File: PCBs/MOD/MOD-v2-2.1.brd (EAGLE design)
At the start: 138.8 x 49.3 mm, 38 parts, among them J1 SERVO1, J10 JOY1, J11 JOY2, J12 RPi-Reset, J2 SERVO2, J3 RPi, J4 ACTUATORS, J5 Battery, J6 AN5, J7 AN6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

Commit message: new MOD pcb
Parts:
- added C1: 10uF, resistor:C0805
- added J13: AN5, SparkFun-Connectors:1X03_LOCK
- added J14: AN6, SparkFun-Connectors:1X03_LOCK
- added J15: AN7, SparkFun-Connectors:1X03_LOCK
- added J16: AN8, SparkFun-Connectors:1X03_LOCK
- J12: value RPi-Reset -> RPi-Shutdown
- J6, J7, J8, J9: device SparkFun-Connectors:1X03_NO_SILK -> SparkFun-Connectors:1X03_LOCK
- R1: device resistor:0204/7 -> rcl:M0805
- R2: value 2.2k -> 2.2K; device resistor:0204/7 -> rcl:M0805
- R3: value 3.3k -> 3.3K; device resistor:0204/7 -> rcl:M0805
- U1: value ATTINY85SU -> ATTINY85
- moved J12 223.1 mm to (127.4, 31.4), flipped to the bottom, turned to 270 degrees
- moved J3 204.9 mm to (150.6, 28.9), turned to 90 degrees
- moved SW2 198.9 mm to (139.6, 7.70), turned to 270 degrees
- moved R3 196.8 mm to (118.1, 12.8), flipped to the bottom
- moved R2 188.3 mm to (118.1, 4.21), flipped to the bottom, turned to 180 degrees
- moved RELAY1 158.8 mm to (131.0, 28.0), flipped to the bottom, turned to 90 degrees
- moved U1 151.6 mm to (128.6, 20.4), flipped to the bottom, turned to 270 degrees
- moved J2 125.3 mm to (2.99, 24.0), flipped to the bottom
- moved J1 120.3 mm to (5.46, 24.0), flipped to the bottom
- moved J9 111.1 mm to (121.3, 34.4), turned to 0 degrees
- moved J4 100.4 mm to (11.0, 32.0)
- moved J8 97.8 mm to (111.1, 34.3), turned to 0 degrees
- moved J6 81.5 mm to (100.8, 34.3), turned to 0 degrees
- moved J7 74.3 mm to (90.5, 34.4), turned to 0 degrees
- moved LED1 70.9 mm to (139.7, 17.9)
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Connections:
- net +3V3: now also J13.1, J14.1, J15.1, J16.1
- net +5V: now also R1.1, TEENSY.VIN; no longer R1.2
- net +5V-BATTERY: now also C1.1
- net AGND: now also J13.2, J14.2, J15.2, J16.2, J6.2, J7.2, J8.2, J9.2; no longer J6.3, J7.3, J8.3, J9.3
- net AN10: now also J7.3
- net AN11: now also J8.3
- net AN12: now also J9.3
- net AN5: now also J13.3; no longer J6.2
- net AN6: now also J14.3; no longer J7.2
- net AN7: now also J15.3; no longer J8.2
- net AN8: now also J16.3; no longer J9.2
- net AN9: now also J6.3
- net GND: now also C1.2, R3.2; no longer R3.1
- net N$2: now also R1.2; no longer R1.1
- net N$5: now also R2.2, R3.1; no longer R2.1, R3.2
- net PI-REST: now also R2.1; no longer R2.2
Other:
- board size 138.8 x 49.3 mm -> 149.8 x 49.3 mm
- board text added: "MOL v2-2"
- board text removed: "MO v2-2"

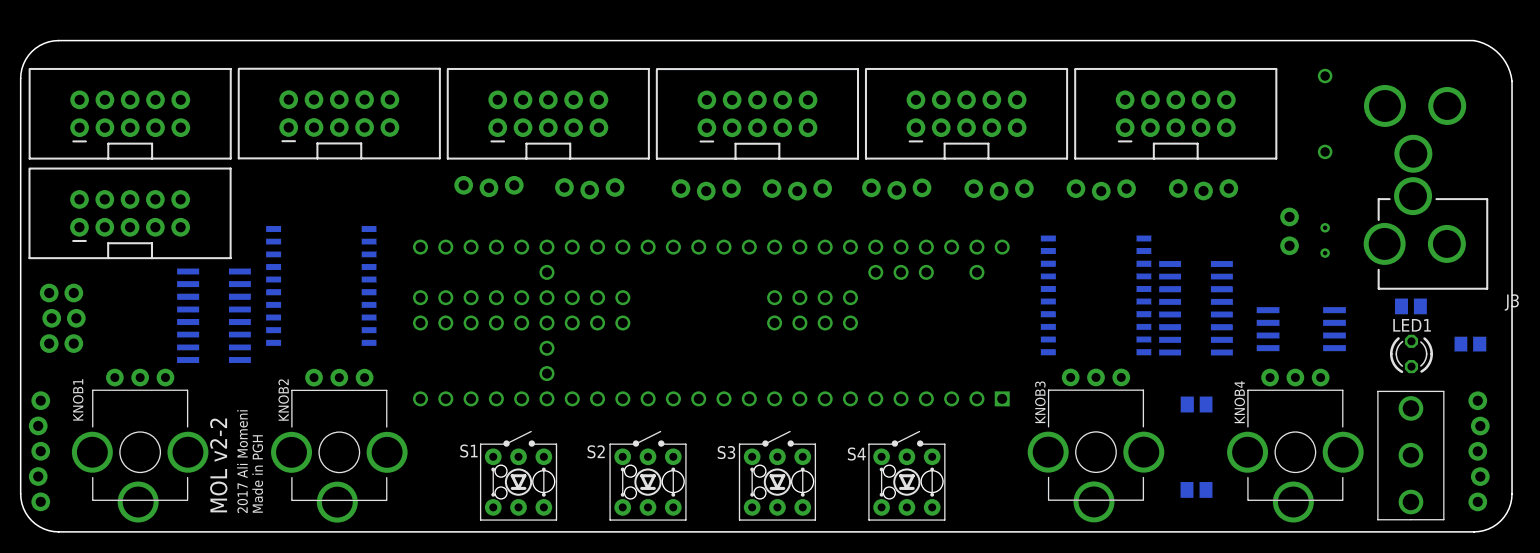
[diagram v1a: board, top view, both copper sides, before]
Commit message: routed new MOD pcb v2-2.1
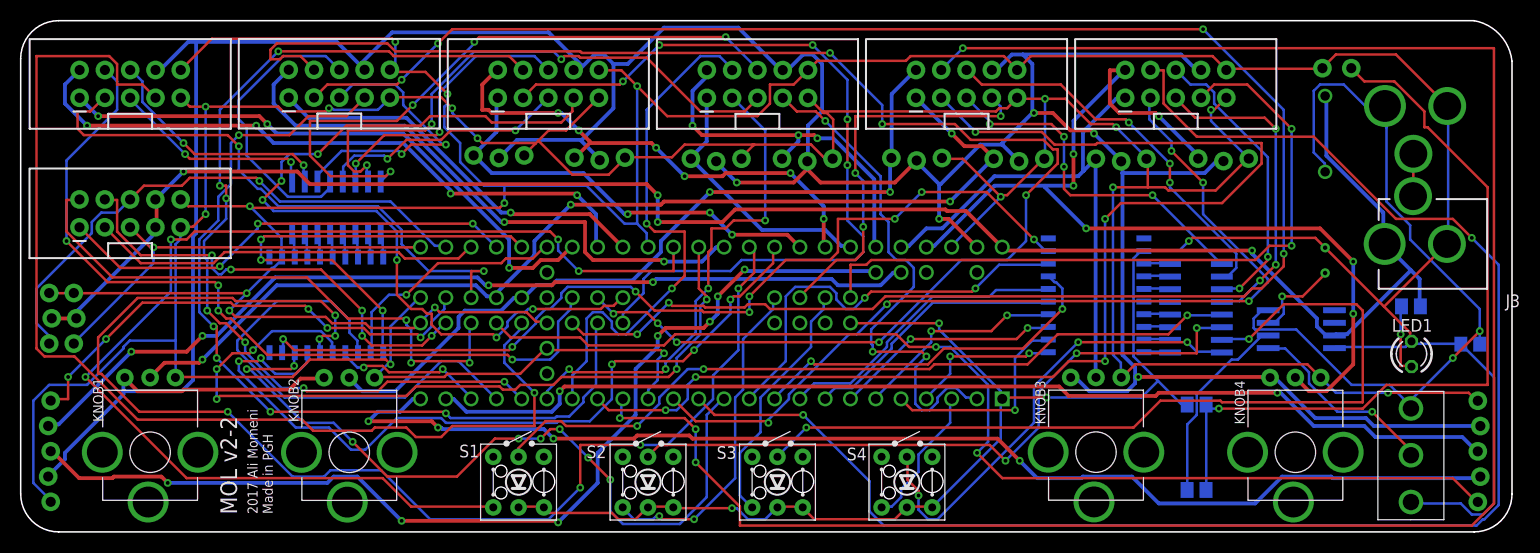
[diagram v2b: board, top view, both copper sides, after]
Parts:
- moved RN2 16.4 mm to (31.7, 32.6), turned to 0 degrees
- moved J12 16.3 mm to (133.4, 46.6), turned to 0 degrees
- moved J6 3.61 mm to (102.8, 37.3)
- moved J7 3.61 mm to (92.5, 37.4)
- moved J8 3.61 mm to (113.1, 37.3)
- moved J9 3.61 mm to (123.3, 37.4)
- moved J13 3.16 mm to (50.6, 37.7)
- moved J14 3.16 mm to (60.7, 37.5)
- moved J15 3.16 mm to (72.4, 37.4)
- moved J16 3.16 mm to (81.5, 37.4)
- moved STRIP1 3.00 mm to (11.0, 45.0)
- moved STRIP2 3.00 mm to (32.0, 45.0)
- moved STRIP3 3.00 mm to (53.0, 45.0)
- moved STRIP4 3.00 mm to (74.0, 45.0)
- moved STRIP5 3.00 mm to (95.0, 45.0)
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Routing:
- net GND: track 0.00 -> 483.5 mm, vias 0 -> 12
- net +3V3: track 0.00 -> 363.2 mm, vias 0 -> 13
- net AGND: track 0.00 -> 355.7 mm, vias 0 -> 5
- net B10: track 0.00 -> 200.5 mm, vias 0 -> 4
- net B3: track 0.00 -> 194.8 mm, vias 0 -> 6
- net +5V: track 0.00 -> 183.1 mm, vias 0 -> 4
- net B12: track 0.00 -> 157.4 mm, vias 0 -> 2
- net B4: track 0.00 -> 150.6 mm, vias 0 -> 7
- net PWM11: track 0.00 -> 128.3 mm, vias 0 -> 7
- net JOYV2: track 0.00 -> 122.9 mm, vias 0 -> 4
- net B9: track 0.00 -> 122.9 mm, vias 0 -> 5
- net B13: track 0.00 -> 119.2 mm, vias 0 -> 4
- net JOYB2: track 0.00 -> 112.5 mm, vias 0 -> 2
- net LED1: track 0.00 -> 111.1 mm, vias 0 -> 1
- net JOYH2: track 0.00 -> 108.9 mm, vias 0 -> 2
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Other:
- board size 149.8 x 49.3 mm -> 149.8 x 51.3 mm
